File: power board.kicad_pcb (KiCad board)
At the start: 2 copper layers, 226.1 x 95.9 mm, 29 parts, among them J1 Conn_01x02_Female, J10 Conn_01x02_Female, J11 Conn_01x02_Female, J12 Conn_01x02_Female, J2 Conn_01x02_Female, J3 Conn_01x02_Female, J4 Conn_01x02_Female, J5 Conn_01x02_Female, J6 Conn_01x02_Female, J7 Conn_01x02_Female, J8 Conn_01x02_Female, J9 Conn_01x02_Female, Q1 STP160N3LL, U1 THL-25-2411

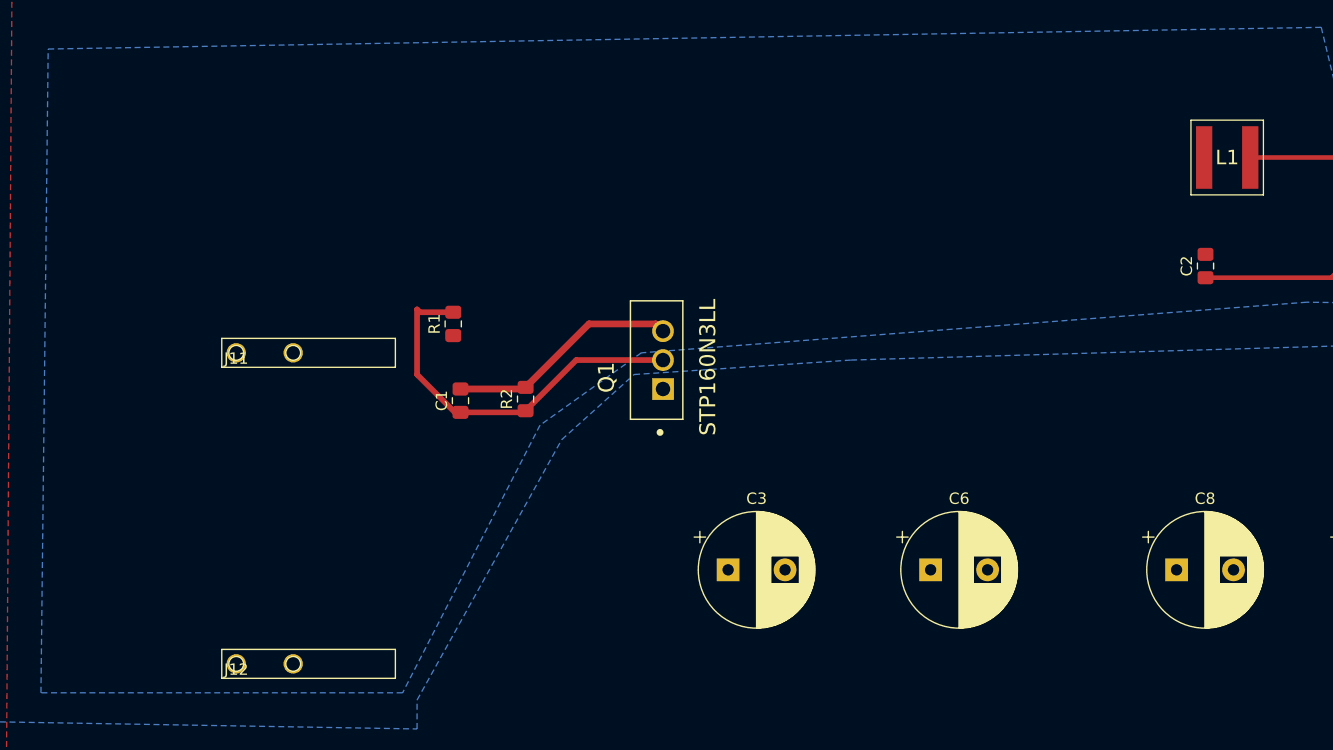
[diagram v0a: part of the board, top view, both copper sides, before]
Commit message: deleted diode and added caps
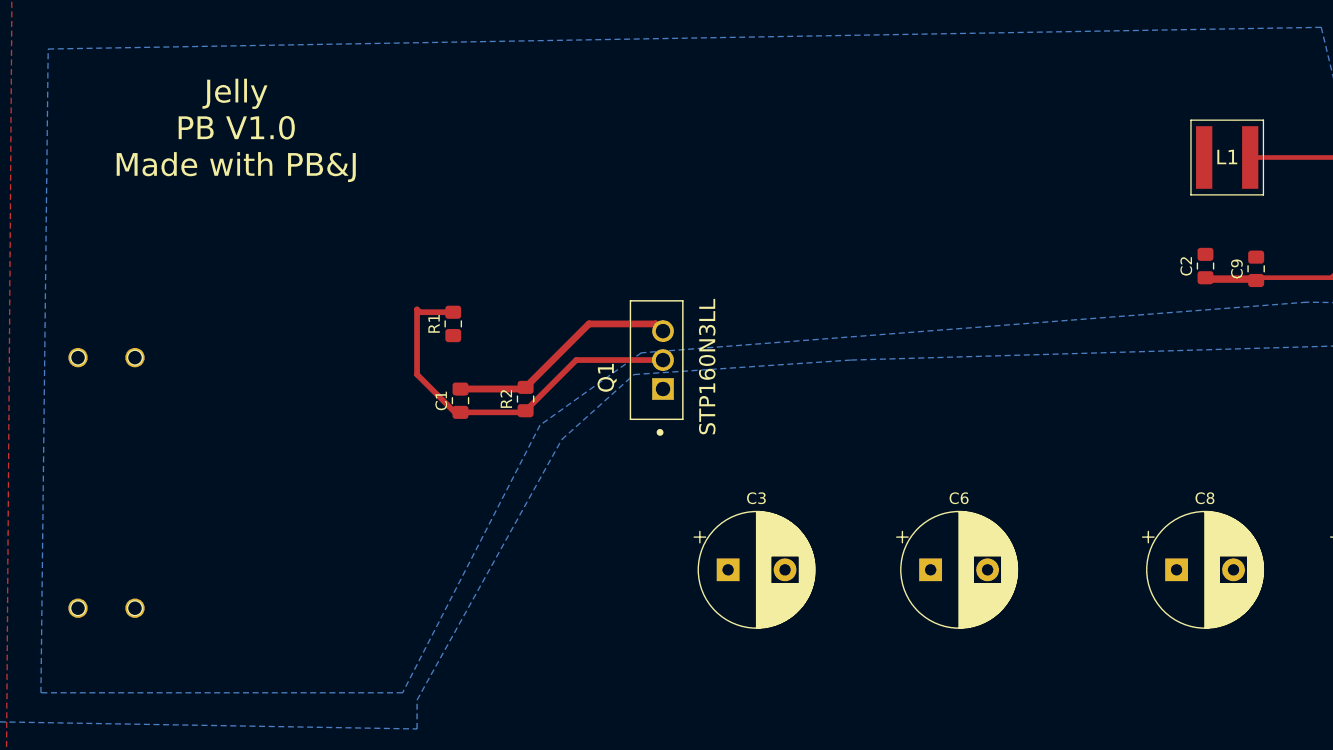
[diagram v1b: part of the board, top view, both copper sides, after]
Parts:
- added C9: 3.3UF, Capacitor_SMD:C_0805_2012Metric_Pad1.15x1.40mm_HandSolder, F.Cu at (136.5, 61.2)
- moved J12 10.1 mm to (38.1, 91.0), turned to 180 degrees
- moved J11 8.90 mm to (38.1, 69.0), turned to 180 degrees
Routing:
- net GND: track 36.5 -> 41.0 mm
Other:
- board text added: "Jelly PB V1.0 Made with PB&J"
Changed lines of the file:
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@@
   (general
     (thickness 1.6)
-    (drawings 20)
-    (tracks 24)
+    (drawings 21)
+    (tracks 26)
     (zones 0)
-    (modules 29)
+    (modules 30)
     (nets 10)
   )
@@
     (0 F.Cu signal)
     (31 B.Cu signal)
-    (32 B.Adhes user hide)
+    (32 B.Adhes user)
     (33 F.Adhes user)
-    (34 B.Paste user hide)
-    (35 F.Paste user hide)
+    (34 B.Paste user)
+    (35 F.Paste user)
     (36 B.SilkS user)
     (37 F.SilkS user)
     (38 B.Mask user)
-    (39 F.Mask user hide)
+    (39 F.Mask user)
     (40 Dwgs.User user)
     (41 Cmts.User user)
-    (42 Eco1.User user hide)
+    (42 Eco1.User user)
     (43 Eco2.User user)
     (44 Edge.Cuts user)
-    (45 Margin user hide)
+    (45 Margin user)
     (46 B.CrtYd user)
     (47 F.CrtYd user)
@@
     (add_net safe-V24)
   )
+  (module Connector:battery_conector_powerpack (layer F.Cu)
+    (at 38.1 91 180)
+    (fp_text reference J12 (at 0 3.175 180) (layer B.SilkS)
+      (effects (font (size 1 1) (thickness 0.15)) (justify mirror))
+    )
+    (fp_text value Conn_01x02_Female (at 1.27 -5.08 180) (layer F.Fab)
+      (effects (font (size 1 1) (thickness 0.15)))
+    )
+    (fp_line (start 13.97 -1.27) (end -1.27 -1.27) (layer B.SilkS) (width 0.12))
+    (fp_line (start 13.97 1.27) (end 13.97 -1.27) (layer B.SilkS) (width 0.12))
+    (fp_line (start -1.27 1.27) (end 13.97 1.27) (layer B.SilkS) (width 0.12))
+    (fp_line (start -1.27 -1.27) (end -1.27 1.27) (layer B.SilkS) (width 0.12))
+    (fp_circle (center 5 0) (end 5.65 0) (layer F.SilkS) (width 0.12))
+    (fp_circle (center 0 0) (end 0.65 0) (layer F.SilkS) (width 0.12))
+    (pad 2 thru_hole circle (at 5 0 180) (size 1.7 1.7) (drill 1.3) (layers *.Cu *.Mask)
+      (net 1 GND))
+    (pad 1 thru_hole circle (at 0 0 180) (size 1.7 1.7) (drill 1.3) (layers *.Cu *.Mask)
+      (net 1 GND))
+  )
+  (module Connector:battery_conector_powerpack (layer F.Cu)
+    (at 38.1 69 180)
+    (fp_text reference J11 (at 1.27 2.58 180) (layer B.SilkS)
+      (effects (font (size 1 1) (thickness 0.15)))
+    )
+    (fp_text value Conn_01x02_Female (at 1.27 -5.08 180) (layer F.Fab)
+      (effects (font (size 1 1) (thickness 0.15)))
+    )
+    (fp_line (start 13.97 -1.27) (end -1.27 -1.27) (layer B.SilkS) (width 0.12))
+    (fp_line (start 13.97 1.27) (end 13.97 -1.27) (layer B.SilkS) (width 0.12))
+    (fp_line (start -1.27 1.27) (end 13.97 1.27) (layer B.SilkS) (width 0.12))
+    (fp_line (start -1.27 -1.27) (end -1.27 1.27) (layer B.SilkS) (width 0.12))
+    (fp_circle (center 5 0) (end 5.65 0) (layer F.SilkS) (width 0.12))
+    (fp_circle (center 0 0) (end 0.65 0) (layer F.SilkS) (width 0.12))
+    (pad 2 thru_hole circle (at 5 0 180) (size 1.7 1.7) (drill 1.3) (layers *.Cu *.Mask)
+      (net 3 +24V))
+    (pad 1 thru_hole circle (at 0 0 180) (size 1.7 1.7) (drill 1.3) (layers *.Cu *.Mask)
+      (net 3 +24V))
+  )
+  (module Capacitor_SMD:C_0805_2012Metric_Pad1.15x1.40mm_HandSolder (layer F.Cu)
+    (at 136.525 61.205 90)
+    (descr "Capacitor SMD 0805 (2012 Metric), square (rectangular) end terminal, IPC_7351 nominal with elongated pad for handsoldering. (Body size source: https://docs.google.com/spreadsheets/d/1BsfQQcO9C6DZCsRaXUlFlo91Tg2WpOkGARC1WS5S8t0/edit?usp=sharing), generated with kicad-footprint-generator")
+    (tags "capacitor handsolder")
+    (attr smd)
+    (fp_text reference C9 (at 0 -1.65 90) (layer F.SilkS)
+      (effects (font (size 1 1) (thickness 0.15)))
+    )
+    (fp_text value 3.3UF (at 0 1.65 90) (layer F.Fab)
+      (effects (font (size 1 1) (thickness 0.15)))
+    )
+    (fp_text user %R (at 0 0 90) (layer F.Fab)
+      (effects (font (size 0.5 0.5) (thickness 0.08)))
+    )
+    (fp_line (start 1.85 0.95) (end -1.85 0.95) (layer F.CrtYd) (width 0.05))
+    (fp_line (start 1.85 -0.95) (end 1.85 0.95) (layer F.CrtYd) (width 0.05))
+    (fp_line (start -1.85 -0.95) (end 1.85 -0.95) (layer F.CrtYd) (width 0.05))
+    (fp_line (start -1.85 0.95) (end -1.85 -0.95) (layer F.CrtYd) (width 0.05))
+    (fp_line (start -0.261252 0.71) (end 0.261252 0.71) (layer F.SilkS) (width 0.12))
+    (fp_line (start -0.261252 -0.71) (end 0.261252 -0.71) (layer F.SilkS) (width 0.12))
+    (fp_line (start 1 0.6) (end -1 0.6) (layer F.Fab) (width 0.1))
+    (fp_line (start 1 -0.6) (end 1 0.6) (layer F.Fab) (width 0.1))
+    (fp_line (start -1 -0.6) (end 1 -0.6) (layer F.Fab) (width 0.1))
+    (fp_line (start -1 0.6) (end -1 -0.6) (layer F.Fab) (width 0.1))
+    (pad 2 smd roundrect (at 1.025 0 90) (size 1.15 1.4) (layers F.Cu F.Paste F.Mask) (roundrect_rratio 0.217391)
+      (net 3 +24V))
+    (pad 1 smd roundrect (at -1.025 0 90) (size 1.15 1.4) (layers F.Cu F.Paste F.Mask) (roundrect_rratio 0.217391)
+      (net 1 GND))
+    (model ${KISYS3DMOD}/Capacitor_SMD.3dshapes/C_0805_2012Metric.wrl
+      (at (xyz 0 0 0))
+      (scale (xyz 1 1 1))
+      (rotate (xyz 0 0 0))
+    )
+  )
   (module TestPoint:TestPoint_THTPad_D3.0mm_Drill1.5mm (layer F.Cu)
     (at 212.09 52.07)
@@
       (net 7 "Net-(L1-Pad2)"))
     (pad 1 smd rect (at -2.02 0) (size 1.43 5.5) (layers F.Cu F.Paste)
-      (net 3 +24V))
-  )
-  (module Connector:battery_conector_powerpack (layer F.Cu)
-    (at 46.99 95.885)
-    (fp_text reference J12 (at 0 0.5) (layer F.SilkS)
-      (effects (font (size 1 1) (thickness 0.15)))
-    )
-    (fp_text value Conn_01x02_Female (at 1.27 -5.08) (layer F.Fab)
-      (effects (font (size 1 1) (thickness 0.15)))
-    )
-    (fp_line (start 13.97 -1.27) (end -1.27 -1.27) (layer F.SilkS) (width 0.12))
-    (fp_line (start 13.97 1.27) (end 13.97 -1.27) (layer F.SilkS) (width 0.12))
-    (fp_line (start -1.27 1.27) (end 13.97 1.27) (layer F.SilkS) (width 0.12))
-    (fp_line (start -1.27 -1.27) (end -1.27 1.27) (layer F.SilkS) (width 0.12))
-    (fp_circle (center 5 0) (end 5.65 0) (layer F.SilkS) (width 0.12))
-    (fp_circle (center 0 0) (end 0.65 0) (layer F.SilkS) (width 0.12))
-    (pad 2 thru_hole circle (at 5 0) (size 1.7 1.7) (drill 1.3) (layers *.Cu *.Mask)
-      (net 1 GND))
-    (pad 1 thru_hole circle (at 0 0) (size 1.7 1.7) (drill 1.3) (layers *.Cu *.Mask)
-      (net 1 GND))
-  )
-  (module Connector:battery_conector_powerpack (layer F.Cu)
-    (at 46.99 68.58)
-    (fp_text reference J11 (at 0 0.5) (layer F.SilkS)
-      (effects (font (size 1 1) (thickness 0.15)))
-    )
-    (fp_text value Conn_01x02_Female (at 1.27 -5.08) (layer F.Fab)
-      (effects (font (size 1 1) (thickness 0.15)))
-    )
-    (fp_line (start 13.97 -1.27) (end -1.27 -1.27) (layer F.SilkS) (width 0.12))
-    (fp_line (start 13.97 1.27) (end 13.97 -1.27) (layer F.SilkS) (width 0.12))
-    (fp_line (start -1.27 1.27) (end 13.97 1.27) (layer F.SilkS) (width 0.12))
-    (fp_line (start -1.27 -1.27) (end -1.27 1.27) (layer F.SilkS) (width 0.12))
-    (fp_circle (center 5 0) (end 5.65 0) (layer F.SilkS) (width 0.12))
-    (fp_circle (center 0 0) (end 0.65 0) (layer F.SilkS) (width 0.12))
-    (pad 2 thru_hole circle (at 5 0) (size 1.7 1.7) (drill 1.3) (layers *.Cu *.Mask)
-      (net 3 +24V))
-    (pad 1 thru_hole circle (at 0 0) (size 1.7 1.7) (drill 1.3) (layers *.Cu *.Mask)
       (net 3 +24V))
   )
@@
     )
   )
+  (gr_text "Jelly\nPB V1.0\nMade with PB&J" (at 46.99 48.895) (layer F.SilkS)
+    (effects (font (size 2 2) (thickness 0.3)))
+  )
   (gr_arc (start 241.935 38.1) (end 247.015 38.1) (angle -90) (layer Edge.Cuts) (width 0.05))
   (gr_line (start 20.955 37.465) (end 20.955 43.18) (layer Edge.Cuts) (width 0.05))
@@
   (segment (start 132.08 61.985) (end 143.12 61.985) (width 0.4) (layer F.Cu) (net 1) (status 400000))
   (segment (start 143.12 61.985) (end 146.685 58.42) (width 0.4) (layer F.Cu) (net 1))
+  (segment (start 132.325 62.23) (end 132.08 61.985) (width 0.4) (layer F.Cu) (net 1))
+  (segment (start 136.525 62.23) (end 132.325 62.23) (width 0.4) (layer F.Cu) (net 1))
   (segment (start 84.455 69.215) (end 76.835 69.215) (width 0.5) (layer F.Cu) (net 2) (status 400000))
   (segment (start 76.835 69.215) (end 72.245 73.805) (width 0.5) (layer F.Cu) (net 2) (status 800000))

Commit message: final V1.0 sent out -gerbers zipped
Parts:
- added H1: MountingHole, MountingHole:MountingHole_3.2mm_M3, F.Cu at (142.0, 118.0)
- added H2: MountingHole, MountingHole:MountingHole_3.2mm_M3, F.Cu at (27.0, 38.0)
- added H3: MountingHole, MountingHole:MountingHole_3.2mm_M3, F.Cu at (27.0, 118.0)
- added H4: MountingHole, MountingHole:MountingHole_3.2mm_M3, F.Cu at (142.0, 38.0)
- moved J8 94.1 mm to (121.3, 106.3)
- moved J10 89.1 mm to (111.1, 106.0)
- moved J9 82.1 mm to (100.3, 106.0)
- moved C4 77.4 mm to (107.3, 78.1)
- moved H21 75.0 mm to (137.2, 62.2)
- moved H22 75.0 mm to (137.2, 54.6)
- moved C2 73.1 mm to (59.7, 51.0)
- moved C9 72.5 mm to (64.8, 51.0)
- moved L1 72.2 mm to (62.2, 43.8)
- moved C7 71.7 mm to (94.0, 78.7)
- moved U1 69.9 mm to (115.6, 47.0)
- moved J3 63.6 mm to (90.8, 106.0)
- moved J1 59.1 mm to (82.5, 106.0)
- moved J7 55.3 mm to (73.7, 106.0)
- moved J5 52.2 mm to (65.4, 106.1)
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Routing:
- net GND: track 41.0 -> 82.3 mm
- net ISO_GND_5V: track 32.8 -> 43.2 mm
- net Net-(R3-Pad1): track 44.2 -> 45.4 mm
- net Net-(L1-Pad2): track 55.6 -> 54.6 mm
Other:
- board size 226.1 x 95.9 mm -> 127.6 x 90.8 mm
- board text added: "+24V"
- board text added: "GND"
- board text added: "ISO_5V"
- board text added: "ISO_GND"
- board text added: "XT30 x 7"
- board text added: "XT60 x 3"
